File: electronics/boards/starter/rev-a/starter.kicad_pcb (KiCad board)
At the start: 2 copper layers, 100 x 85 mm, 41 parts, among them J1 USB-C DEVICE, J2 12V CAN - NOT PHONE, J3 12V CAN - NOT PHONE, J4 SWD / 3V3 REFERENCE ONLY, J5 GPIO 3V3, J6 CAN TEST / END TERMINATION, SW1 TEST BUTTON, SW2 RESET, U1 STM32G0B1CBT6, U2 USBLC6-2SC6, U3 TCAN3413D, U4 R-78E5.0-0.5, U5 TLV75533PDBVR

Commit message: Add representative button, axis, hat, encoder and switch examples
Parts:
- added C12: 100nF 25V X7R, KiCad:C_0805_2012Metric, F.Cu at (114.0, 138.0)
- added J10: 3-POSITION SELECTOR, KiCad:PinHeader_1x03_P2.54mm_Vertical, F.Cu at (177.0, 123.0)
- added J7: HAT N E S W, KiCad:PinHeader_1x05_P2.54mm_Vertical, F.Cu at (114.0, 106.0)
- added J8: ENCODER A B PUSH, KiCad:PinHeader_1x04_P2.54mm_Vertical, F.Cu at (164.0, 102.0)
- added J9: MAINTAINED TOGGLE, KiCad:PinHeader_1x02_P2.54mm_Vertical, F.Cu at (177.0, 108.0)
- added R10: 10k, KiCad:R_0805_2012Metric, F.Cu at (121.0, 109.0)
- added R11: 10k, KiCad:R_0805_2012Metric, F.Cu at (121.0, 113.0)
- added R12: 10k, KiCad:R_0805_2012Metric, F.Cu at (121.0, 117.0)
- added R13: 10k, KiCad:R_0805_2012Metric, F.Cu at (161.0, 115.0)
- added R14: 10k, KiCad:R_0805_2012Metric, F.Cu at (165.0, 115.0)
- added R15: 10k, KiCad:R_0805_2012Metric, F.Cu at (169.0, 115.0)
- added R16: 10k, KiCad:R_0805_2012Metric, F.Cu at (177.0, 116.0)
- added R17: 10k, KiCad:R_0805_2012Metric, F.Cu at (183.0, 124.0)
- added R18: 10k, KiCad:R_0805_2012Metric, F.Cu at (183.0, 129.0)
- added R19: 1k, KiCad:R_0805_2012Metric, F.Cu at (119.0, 136.0)
- added R20: 1M, KiCad:R_0805_2012Metric, F.Cu at (114.0, 143.0)
- added R21: 1M, KiCad:R_0805_2012Metric, F.Cu at (114.0, 147.0)
- added R9: 10k, KiCad:R_0805_2012Metric, F.Cu at (121.0, 105.0)
- J5: value GPIO 3V3 -> 10k LINEAR AXIS POT; footprint KiCad:PinHeader_1x06_P2.54mm_Vertical -> KiCad:PinHeader_1x03_P2.54mm_Vertical
- moved J5 8.60 mm to (114.0, 125.0)
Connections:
- net /+3V3 renamed +3V3
- C1 pad 2: /GND -> GND
- C10 pad 2: /GND -> GND
- C11 pad 2: /GND -> GND
- C2 pad 2: /GND -> GND
- C3 pad 2: /GND -> GND
- C4 pad 2: /GND -> GND
- C5 pad 2: /GND -> GND
- C6 pad 2: /GND -> GND
- C7 pad 2: /GND -> GND
- C8 pad 2: /GND -> GND
- C9 pad 2: /GND -> GND
- D4 pad 1: /GND -> GND
- J1 pad A1: /GND -> GND
- J1 pad A12: /GND -> GND
- J1 pad B1: /GND -> GND
- J1 pad B12: /GND -> GND
- J1 pad SH: /GND -> GND
- J2 pad 2: /GND -> GND
- J2 pad 5: /GND -> GND
- J3 pad 2: /GND -> GND
- J3 pad 5: /GND -> GND
- J4 pad 2: /GND -> GND
- J5 pad 2: /GND -> AXIS_WIPER
- J5 pad 3: /PA1 -> GND
- J6 pad 3: /GND -> GND
- R1 pad 2: /GND -> GND
- R2 pad 2: /GND -> GND
- R4 pad 2: /GND -> GND
- SW1 pad 2: /GND -> GND
- SW2 pad 2: /GND -> GND
- U1 pad 12: /PA1 -> AXIS_ADC
- U1 pad 13: /PA2 -> HAT_N
- U1 pad 14: /PA3 -> HAT_E
- U1 pad 15: /PA4 -> HAT_S
- U1 pad 17: unconnected-(U1-PA6-Pad17) -> HAT_W
- U1 pad 18: unconnected-(U1-PA7-Pad18) -> ENC_A
- U1 pad 20: unconnected-(U1-PB1-Pad20) -> TOGGLE
- U1 pad 21: unconnected-(U1-PB2-Pad21) -> SELECT_LOW
- U1 pad 28: unconnected-(U1-PA8-Pad28) -> ENC_B
- U1 pad 37: unconnected-(U1-PA15-Pad37) -> ENC_PUSH
- U1 pad 42: unconnected-(U1-PB3-Pad42) -> SELECT_HIGH
- U1 pad 7: /GND -> GND
- U2 pad 2: /GND -> GND
- U3 pad 2: /GND -> GND
- U4 pad 2: /GND -> GND
- U5 pad 2: /GND -> GND
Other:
- board text removed: "GPIO 3V3"

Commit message: Route STM32G0B1 starter PCB and verify copper connectivity
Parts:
- moved D3 31.8 mm to (137.0, 144.0)
- moved J6 29.4 mm to (187.0, 132.0)
- moved C12 23.7 mm to (137.5, 141.0)
- moved R2 20.2 mm to (134.0, 104.0)
- moved C1 19.8 mm to (181.0, 126.5), turned to 90 degrees
- moved R21 16.6 mm to (130.5, 145.0)
- moved U3 16.3 mm to (186.0, 126.0)
- moved R20 14.6 mm to (128.5, 141.0)
- moved R5 14.4 mm to (183.0, 122.0)
- moved R19 14.4 mm to (132.5, 141.0)
- moved C2 13.8 mm to (115.5, 153.0), turned to 180 degrees
- moved F1 13.0 mm to (126.0, 145.0), turned to 180 degrees
- moved C8 12.4 mm to (132.5, 133.0)
- moved R1 10.4 mm to (147.0, 108.0)
- moved D1 8.49 mm to (120.0, 147.0)
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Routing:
- net +3V3: track 0.00 -> 217.2 mm, vias 0 -> 7
- net /BUS_12V: track 0.00 -> 127.5 mm, vias 0 -> 2
- net /CAN_TX: track 0.00 -> 85.0 mm, vias 0 -> 2
- net ENC_A: track 0.00 -> 82.6 mm, vias 0 -> 2
- net /USB_VBUS: track 0.00 -> 82.1 mm, vias 0 -> 6
- net /CAN_RX: track 0.00 -> 81.1 mm, vias 0 -> 2
- net GND: track 0.00 -> 71.7 mm, vias 0 -> 81
- net /NRST: track 0.00 -> 67.7 mm, vias 0 -> 2
- net /CAN_STB: track 0.00 -> 66.1 mm, vias 0 -> 2
- net TOGGLE: track 0.00 -> 58.1 mm, vias 0 -> 1
- net ENC_PUSH: track 0.00 -> 57.5 mm, vias 0 -> 1
- net /BUTTON: track 0.00 -> 56.9 mm, vias 0 -> 2
- net HAT_N: track 0.00 -> 56.7 mm, vias 0 -> 1
- net /SWCLK: track 0.00 -> 55.4 mm, vias 0 -> 1
- net /CAN_L: track 0.00 -> 53.7 mm, vias 0 -> 2
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- added copper zone on B.Cu, net GND
- added copper zone on F.Cu, net GND
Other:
- board text added: "REV A - ROUTED PROTOTYPE"
- board text removed: "REV A - UNROUTED DRAFT"

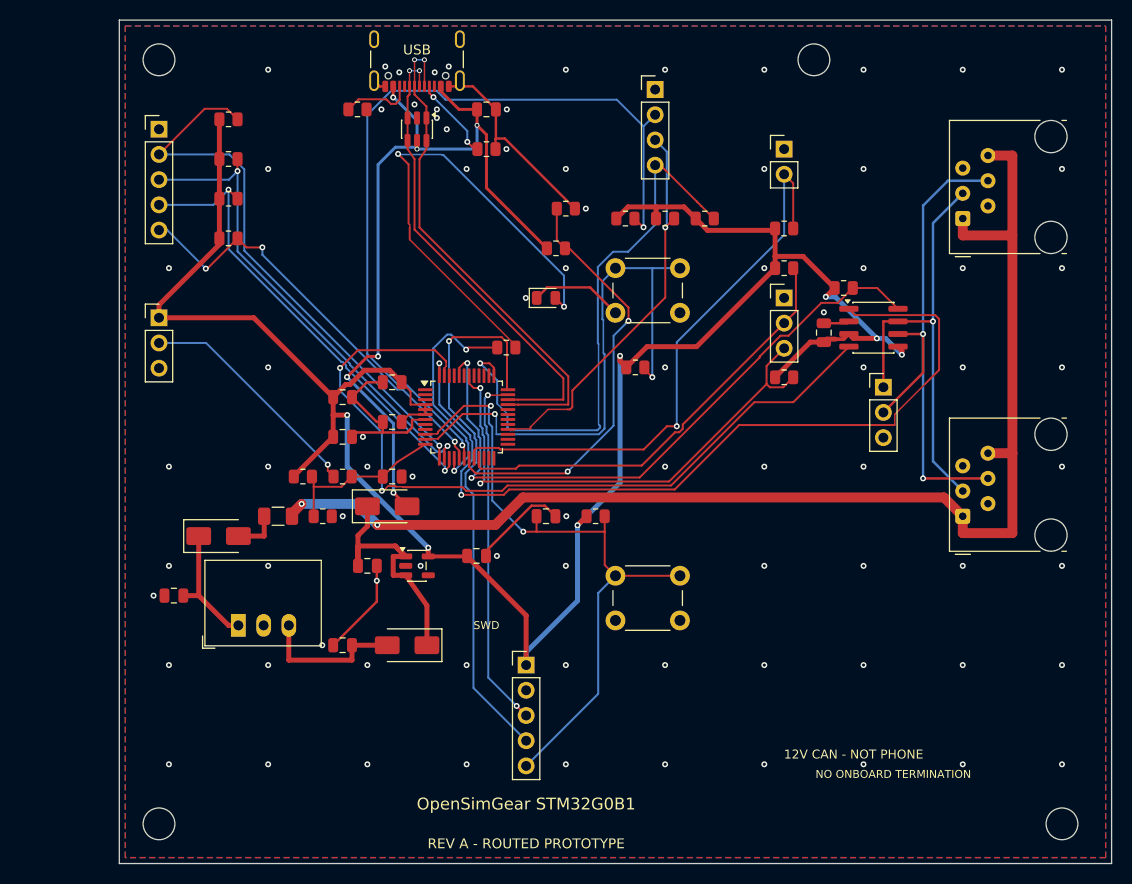
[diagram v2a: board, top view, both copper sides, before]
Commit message: Review compact four-layer PCB and add milling qualification coupon
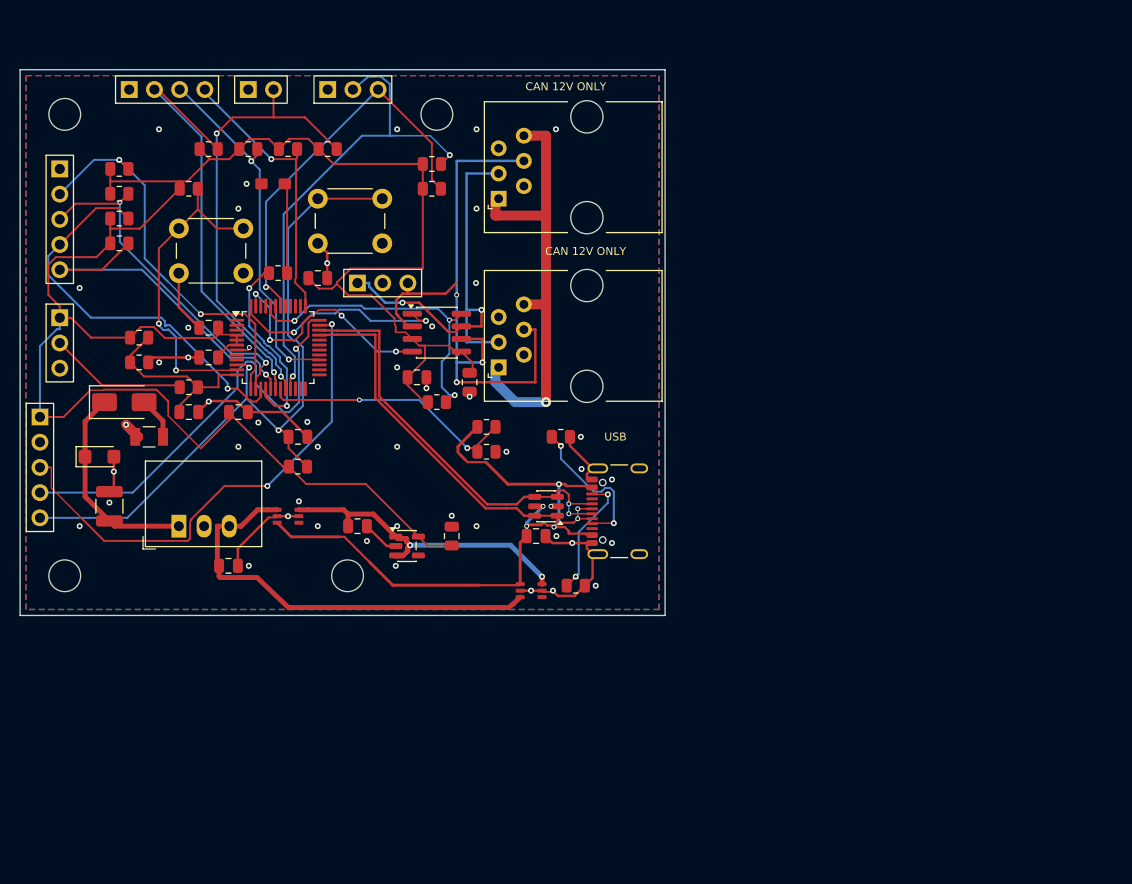
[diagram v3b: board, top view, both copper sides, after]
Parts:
- removed D2, D3: SS14, KiCad:D_SMA
- added C13: 100nF 25V X7R, KiCad:C_0805_2012Metric, F.Cu at (145.3, 131.5)
- added D5: SMF15A-E3-08, KiCad:D_SMF, F.Cu at (108.0, 139.0)
- added U6: LM66100DCKR, OpenSimGear:TI_DCK0006A_SC70-6_LM66100, F.Cu at (127.0, 145.0)
- added U7: LM66100DCKR, OpenSimGear:TI_DCK0006A_SC70-6_LM66100, F.Cu at (151.5, 152.5)
- C2: footprint KiCad:C_0805_2012Metric -> KiCad:C_1210_3225Metric
- C5: value 1uF 25V X7R -> 2.2uF 25V X7R
- D4: footprint KiCad:LED_0805_2012Metric -> OpenSimGear:LED_Kingbright_AP2012SGC_0805
- F1: value 0.25A hold / 30V -> 0.25A hold / 24V; footprint KiCad:Fuse_1206_3216Metric -> OpenSimGear:Fuse_Littelfuse_1206L025-24YR
- J10, J5, J6: footprint KiCad:PinHeader_1x03_P2.54mm_Vertical -> OpenSimGear:PinHeader_Samtec_TSW-103-07-L-S_P2.54mm_Vertical
- J2, J3: footprint KiCad:RJ12_Amphenol_54601-x06_Horizontal -> OpenSimGear:RJ12_Amphenol_RJE051660510H_Horizontal
- J4, J7: footprint KiCad:PinHeader_1x05_P2.54mm_Vertical -> OpenSimGear:PinHeader_Samtec_TSW-105-07-L-S_P2.54mm_Vertical
- J8: footprint KiCad:PinHeader_1x04_P2.54mm_Vertical -> OpenSimGear:PinHeader_Samtec_TSW-104-07-L-S_P2.54mm_Vertical
- J9: footprint KiCad:PinHeader_1x02_P2.54mm_Vertical -> OpenSimGear:PinHeader_Samtec_TSW-102-07-L-S_P2.54mm_Vertical
- SW1, SW2: footprint KiCad:SW_PUSH_6mm_H5mm -> KiCad:SW_PUSH_6mm_H4.3mm
- moved H4 76.2 mm to (133.0, 151.0)
- moved J4 55.0 mm to (102.0, 135.0)
- moved J9 54.3 mm to (123.0, 102.0), turned to 90 degrees
- moved J6 54.0 mm to (134.0, 121.5), turned to 90 degrees
- moved J8 53.0 mm to (111.0, 102.0), turned to 90 degrees
- moved R2 52.8 mm to (156.0, 152.0)
- moved J1 51.2 mm to (161.3, 144.5), turned to 90 degrees
- moved J10 50.6 mm to (131.0, 102.0), turned to 90 degrees
- moved J3 49.1 mm to (148.2, 130.0)
- moved R6 48.5 mm to (117.0, 112.0)
- moved SW2 48.4 mm to (130.0, 113.0)
- moved J2 46.8 mm to (148.2, 113.0)
- moved R16 46.7 mm to (131.0, 108.0)
- moved SW1 44.2 mm to (116.0, 116.0)
- moved U3 44.0 mm to (142.0, 126.5)
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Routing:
- net /CAN_TX: track 85.0 -> 22.3 mm
- net /CAN_RX: track 81.1 -> 24.4 mm, vias 2 -> 4
- net /LED_K: track 50.7 -> 9.10 mm, vias 2 -> 0
- net ENC_A: track 82.6 -> 44.2 mm, vias 2 -> 1
- net /BUS_12V: track 127.5 -> 92.3 mm
- net /CAN_STB: track 66.1 -> 32.0 mm, vias 2 -> 3
- net /BUCK_5V: track 14.9 -> 43.8 mm
- net ENC_PUSH: track 57.5 -> 28.6 mm
- net /BUTTON: track 56.9 -> 32.5 mm
- net /VBUS_SENSE: track 43.4 -> 26.0 mm
- net HAT_N: track 56.7 -> 40.3 mm, vias 1 -> 2
- net /SWDIO: track 36.2 -> 50.9 mm
- net +3V3: track 217.2 -> 202.8 mm, vias 7 -> 0
- net HAT_E: track 48.8 -> 34.8 mm
- net /USB_VBUS: track 82.1 -> 68.3 mm, vias 6 -> 4
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- added copper zone on In1.Cu, net GND
- added copper zone on In2.Cu, net GND
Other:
- board size 100 x 85 mm -> 65 x 55 mm
- copper layers 2 -> 4
- board text added: "CAN 12V ONLY"
- board text added: "OpenSimGear"
- board text removed: "12V CAN - NOT PHONE"
- board text removed: "NO ONBOARD TERMINATION"
- board text removed: "OpenSimGear STM32G0B1"
- board text removed: "REV A - ROUTED PROTOTYPE"
- board text removed: "SWD"
